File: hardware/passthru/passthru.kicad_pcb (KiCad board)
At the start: 2 copper layers, 63.5 x 59.7 mm, 83 parts, among them J1 ARM_SWD, J2 RJ45_LED_Shielded, J3 Screw_Terminal_01x02, Q1 Q_PMOS_DGS, Q2 Q_PMOS_DGS, Q3 Q_NPN_BEC, U1 EFM32GG11B8xx, U2 KSZ8081RND, U3 LM5085, U4 TPS2375-1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

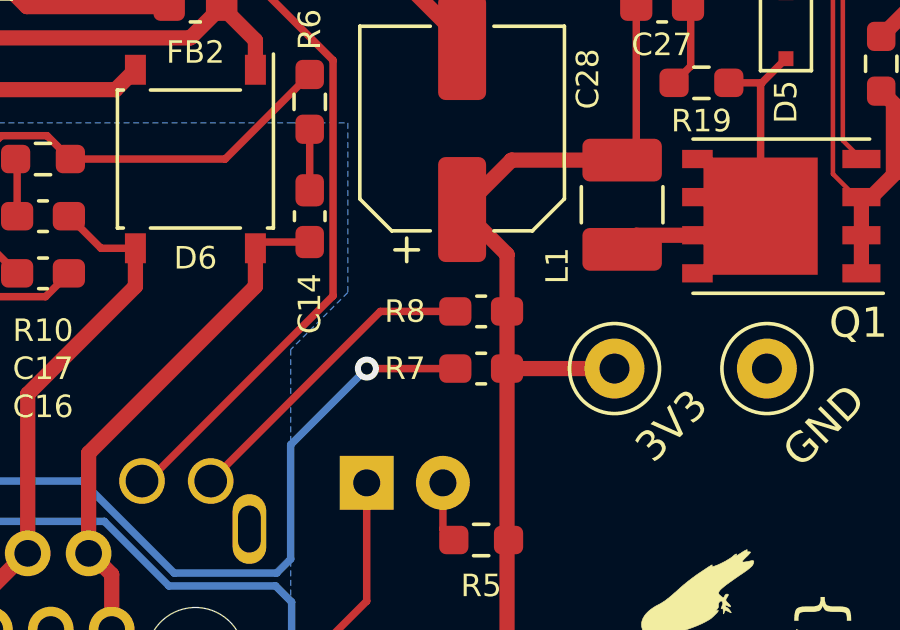
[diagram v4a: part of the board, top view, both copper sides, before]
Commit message: passthru: update resistor values
The 6.1 kΩ resistor was hard to find. I also added the
current-limiting resistors for the LEDs.
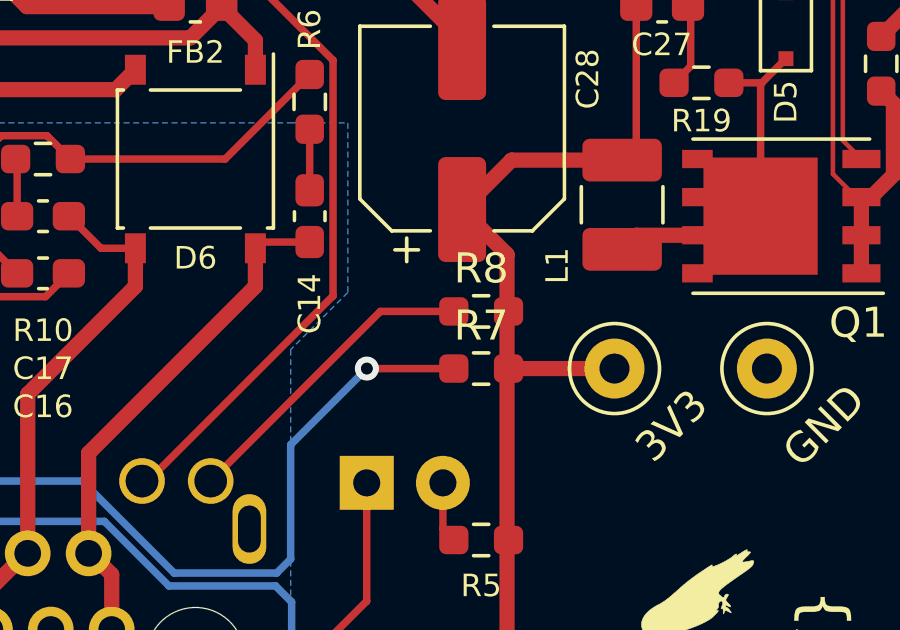
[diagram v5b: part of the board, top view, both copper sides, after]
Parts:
- R20: value 10k -> 16k5
- R21: value 6k1 -> 10k
- R4, R5: value ? -> 68R
- R7, R8: value 65 -> 68R; footprint Capacitor_SMD:C_0603_1608Metric_Pad1.08x0.95mm_HandSolder -> Resistor_SMD:R_0603_1608Metric_Pad0.98x0.95mm_HandSolder
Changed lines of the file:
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@@
       (effects (font (size 0.75 0.75) (thickness 0.15)))
     )
-    (fp_text value "?" (at 0 1.43) (layer "F.Fab")
+    (fp_text value "68R" (at 0 1.43) (layer "F.Fab")
       (effects (font (size 1 1) (thickness 0.15)))
     )
@@
       (effects (font (size 0.75 0.75) (thickness 0.15)))
     )
-    (fp_text value "10k" (at 0 1.43 90) (layer "F.Fab")
+    (fp_text value "16k5" (at 0 1.43 90) (layer "F.Fab")
       (effects (font (size 1 1) (thickness 0.15)))
     )
@@
     )
   )
-  (footprint "Capacitor_SMD:C_0603_1608Metric_Pad1.08x0.95mm_HandSolder" (layer "F.Cu")
+  (footprint "Resistor_SMD:R_0603_1608Metric_Pad0.98x0.95mm_HandSolder" (layer "F.Cu")
     (at 161.925 85.725)
-    (descr "Capacitor SMD 0603 (1608 Metric), square (rectangular) end terminal, IPC_7351 nominal with elongated pad for handsoldering. (Body size source: IPC-SM-782 page 76, https://www.pcb-3d.com/wordpress/wp-content/uploads/ipc-sm-782a_amendment_1_and_2.pdf), generated with kicad-footprint-generator")
-    (tags "capacitor handsolder")
-    (property "Sheetfile" "passthru.kicad_sch")
-    (property "Sheetname" "")
-    (attr smd)
-    (fp_text reference "R8" (at -2.54 0) (layer "F.SilkS")
-      (effects (font (size 0.75 0.75) (thickness 0.15)))
-    )
-    (fp_text value "65" (at 0 1.43) (layer "F.Fab")
-      (effects (font (size 1 1) (thickness 0.15)))
-    )
-    (fp_text user "${REFERENCE}" (at 0 0) (layer "F.Fab")
-      (effects (font (size 0.4 0.4) (thickness 0.06)))
-    )
-    (fp_line (start -0.146267 -0.51) (end 0.146267 -0.51) (layer "F.SilkS") (width 0.12))
-    (fp_line (start -0.146267 0.51) (end 0.146267 0.51) (layer "F.SilkS") (width 0.12))
-    (fp_line (start 1.65 0.73) (end -1.65 0.73) (layer "F.CrtYd") (width 0.05))
-    (fp_line (start 1.65 -0.73) (end 1.65 0.73) (layer "F.CrtYd") (width 0.05))
-    (fp_line (start -1.65 -0.73) (end 1.65 -0.73) (layer "F.CrtYd") (width 0.05))
-    (fp_line (start -1.65 0.73) (end -1.65 -0.73) (layer "F.CrtYd") (width 0.05))
-    (fp_line (start 0.8 -0.4) (end 0.8 0.4) (layer "F.Fab") (width 0.1))
-    (fp_line (start -0.8 0.4) (end -0.8 -0.4) (layer "F.Fab") (width 0.1))
-    (fp_line (start 0.8 0.4) (end -0.8 0.4) (layer "F.Fab") (width 0.1))
-    (fp_line (start -0.8 -0.4) (end 0.8 -0.4) (layer "F.Fab") (width 0.1))
-    (pad "1" smd roundrect (at -0.8625 0) (size 1.075 0.95) (layers "F.Cu" "F.Paste" "F.Mask") (roundrect_rratio 0.25)
+    (descr "Resistor SMD 0603 (1608 Metric), square (rectangular) end terminal, IPC_7351 nominal with elongated pad for handsoldering. (Body size source: IPC-SM-782 page 72, https://www.pcb-3d.com/wordpress/wp-content/uploads/ipc-sm-782a_amendment_1_and_2.pdf), generated with kicad-footprint-generator")
+    (tags "resistor handsolder")
+    (property "Sheetfile" "passthru.kicad_sch")
+    (property "Sheetname" "")
+    (attr smd)
+    (fp_text reference "R8" (at 0 -1.43) (layer "F.SilkS")
+      (effects (font (size 1 1) (thickness 0.15)))
+    )
+    (fp_text value "68R" (at 0 1.43) (layer "F.Fab")
+      (effects (font (size 1 1) (thickness 0.15)))
+    )
+    (fp_text user "${REFERENCE}" (at 0 0) (layer "F.Fab")
+      (effects (font (size 0.4 0.4) (thickness 0.06)))
+    )
+    (fp_line (start -0.254724 0.5225) (end 0.254724 0.5225) (layer "F.SilkS") (width 0.12))
+    (fp_line (start -0.254724 -0.5225) (end 0.254724 -0.5225) (layer "F.SilkS") (width 0.12))
+    (fp_line (start 1.65 0.73) (end -1.65 0.73) (layer "F.CrtYd") (width 0.05))
+    (fp_line (start -1.65 -0.73) (end 1.65 -0.73) (layer "F.CrtYd") (width 0.05))
+    (fp_line (start -1.65 0.73) (end -1.65 -0.73) (layer "F.CrtYd") (width 0.05))
+    (fp_line (start 1.65 -0.73) (end 1.65 0.73) (layer "F.CrtYd") (width 0.05))
+    (fp_line (start 0.8 0.4125) (end -0.8 0.4125) (layer "F.Fab") (width 0.1))
+    (fp_line (start 0.8 -0.4125) (end 0.8 0.4125) (layer "F.Fab") (width 0.1))
+    (fp_line (start -0.8 0.4125) (end -0.8 -0.4125) (layer "F.Fab") (width 0.1))
+    (fp_line (start -0.8 -0.4125) (end 0.8 -0.4125) (layer "F.Fab") (width 0.1))
+    (pad "1" smd roundrect (at -0.9125 0) (size 0.975 0.95) (layers "F.Cu" "F.Paste" "F.Mask") (roundrect_rratio 0.25)
       (net 97 "Net-(J2-Pad12)") (pintype "passive"))
-    (pad "2" smd roundrect (at 0.8625 0) (size 1.075 0.95) (layers "F.Cu" "F.Paste" "F.Mask") (roundrect_rratio 0.25)
+    (pad "2" smd roundrect (at 0.9125 0) (size 0.975 0.95) (layers "F.Cu" "F.Paste" "F.Mask") (roundrect_rratio 0.25)
       (net 10 "+3V3") (pintype "passive"))
-    (model "${KICAD6_3DMODEL_DIR}/Capacitor_SMD.3dshapes/C_0603_1608Metric.wrl"
+    (model "${KICAD6_3DMODEL_DIR}/Resistor_SMD.3dshapes/R_0603_1608Metric.wrl"
       (offset (xyz 0 0 0))
       (scale (xyz 1 1 1))
@@
     )
   )
-  (footprint "Capacitor_SMD:C_0603_1608Metric_Pad1.08x0.95mm_HandSolder" (layer "F.Cu")
+  (footprint "Resistor_SMD:R_0603_1608Metric_Pad0.98x0.95mm_HandSolder" (layer "F.Cu")
     (at 161.925 87.63)
-    (descr "Capacitor SMD 0603 (1608 Metric), square (rectangular) end terminal, IPC_7351 nominal with elongated pad for handsoldering. (Body size source: IPC-SM-782 page 76, https://www.pcb-3d.com/wordpress/wp-content/uploads/ipc-sm-782a_amendment_1_and_2.pdf), generated with kicad-footprint-generator")
-    (tags "capacitor handsolder")
-    (property "Sheetfile" "passthru.kicad_sch")
-    (property "Sheetname" "")
-    (attr smd)
-    (fp_text reference "R7" (at -2.54 0) (layer "F.SilkS")
-      (effects (font (size 0.75 0.75) (thickness 0.15)))
-    )
-    (fp_text value "65" (at 0 1.43) (layer "F.Fab")
-      (effects (font (size 1 1) (thickness 0.15)))
-    )
-    (fp_text user "${REFERENCE}" (at 0 0) (layer "F.Fab")
-      (effects (font (size 0.4 0.4) (thickness 0.06)))
-    )
-    (fp_line (start -0.146267 -0.51) (end 0.146267 -0.51) (layer "F.SilkS") (width 0.12))
-    (fp_line (start -0.146267 0.51) (end 0.146267 0.51) (layer "F.SilkS") (width 0.12))
-    (fp_line (start 1.65 -0.73) (end 1.65 0.73) (layer "F.CrtYd") (width 0.05))
-    (fp_line (start -1.65 0.73) (end -1.65 -0.73) (layer "F.CrtYd") (width 0.05))
-    (fp_line (start -1.65 -0.73) (end 1.65 -0.73) (layer "F.CrtYd") (width 0.05))
-    (fp_line (start 1.65 0.73) (end -1.65 0.73) (layer "F.CrtYd") (width 0.05))
-    (fp_line (start 0.8 -0.4) (end 0.8 0.4) (layer "F.Fab") (width 0.1))
-    (fp_line (start -0.8 0.4) (end -0.8 -0.4) (layer "F.Fab") (width 0.1))
-    (fp_line (start 0.8 0.4) (end -0.8 0.4) (layer "F.Fab") (width 0.1))
-    (fp_line (start -0.8 -0.4) (end 0.8 -0.4) (layer "F.Fab") (width 0.1))
-    (pad "1" smd roundrect (at -0.8625 0) (size 1.075 0.95) (layers "F.Cu" "F.Paste" "F.Mask") (roundrect_rratio 0.25)
+    (descr "Resistor SMD 0603 (1608 Metric), square (rectangular) end terminal, IPC_7351 nominal with elongated pad for handsoldering. (Body size source: IPC-SM-782 page 72, https://www.pcb-3d.com/wordpress/wp-content/uploads/ipc-sm-782a_amendment_1_and_2.pdf), generated with kicad-footprint-generator")
+    (tags "resistor handsolder")
+    (property "Sheetfile" "passthru.kicad_sch")
+    (property "Sheetname" "")
+    (attr smd)
+    (fp_text reference "R7" (at 0 -1.43) (layer "F.SilkS")
+      (effects (font (size 1 1) (thickness 0.15)))
+    )
+    (fp_text value "68R" (at 0 1.43) (layer "F.Fab")
+      (effects (font (size 1 1) (thickness 0.15)))
+    )
+    (fp_text user "${REFERENCE}" (at 0 0) (layer "F.Fab")
+      (effects (font (size 0.4 0.4) (thickness 0.06)))
+    )
+    (fp_line (start -0.254724 0.5225) (end 0.254724 0.5225) (layer "F.SilkS") (width 0.12))
+    (fp_line (start -0.254724 -0.5225) (end 0.254724 -0.5225) (layer "F.SilkS") (width 0.12))
+    (fp_line (start 1.65 -0.73) (end 1.65 0.73) (layer "F.CrtYd") (width 0.05))
+    (fp_line (start -1.65 -0.73) (end 1.65 -0.73) (layer "F.CrtYd") (width 0.05))
+    (fp_line (start -1.65 0.73) (end -1.65 -0.73) (layer "F.CrtYd") (width 0.05))
+    (fp_line (start 1.65 0.73) (end -1.65 0.73) (layer "F.CrtYd") (width 0.05))
+    (fp_line (start -0.8 0.4125) (end -0.8 -0.4125) (layer "F.Fab") (width 0.1))
+    (fp_line (start 0.8 -0.4125) (end 0.8 0.4125) (layer "F.Fab") (width 0.1))
+    (fp_line (start -0.8 -0.4125) (end 0.8 -0.4125) (layer "F.Fab") (width 0.1))
+    (fp_line (start 0.8 0.4125) (end -0.8 0.4125) (layer "F.Fab") (width 0.1))
+    (pad "1" smd roundrect (at -0.9125 0) (size 0.975 0.95) (layers "F.Cu" "F.Paste" "F.Mask") (roundrect_rratio 0.25)
       (net 96 "Net-(J2-Pad10)") (pintype "passive"))
-    (pad "2" smd roundrect (at 0.8625 0) (size 1.075 0.95) (layers "F.Cu" "F.Paste" "F.Mask") (roundrect_rratio 0.25)
+    (pad "2" smd roundrect (at 0.9125 0) (size 0.975 0.95) (layers "F.Cu" "F.Paste" "F.Mask") (roundrect_rratio 0.25)
       (net 10 "+3V3") (pintype "passive"))
-    (model "${KICAD6_3DMODEL_DIR}/Capacitor_SMD.3dshapes/C_0603_1608Metric.wrl"
+    (model "${KICAD6_3DMODEL_DIR}/Resistor_SMD.3dshapes/R_0603_1608Metric.wrl"
       (offset (xyz 0 0 0))
       (scale (xyz 1 1 1))
@@
       (effects (font (size 0.75 0.75) (thickness 0.15)) (justify left))
     )
-    (fp_text value "6k1" (at 0 1.43) (layer "F.Fab")
+    (fp_text value "10k" (at 0 1.43) (layer "F.Fab")
       (effects (font (size 1 1) (thickness 0.15)))
     )
@@
       (effects (font (size 0.75 0.75) (thickness 0.15)))
     )
-    (fp_text value "?" (at 0 1.43) (layer "F.Fab")
-      (effects (font (size 1 1) (thickness 0.15)))
-    )
+    (fp_text value "68R" (at 0 1.43) (layer "F.Fab")
+      (effects (font (size 1 1) (thickness 0.15)))
+    )

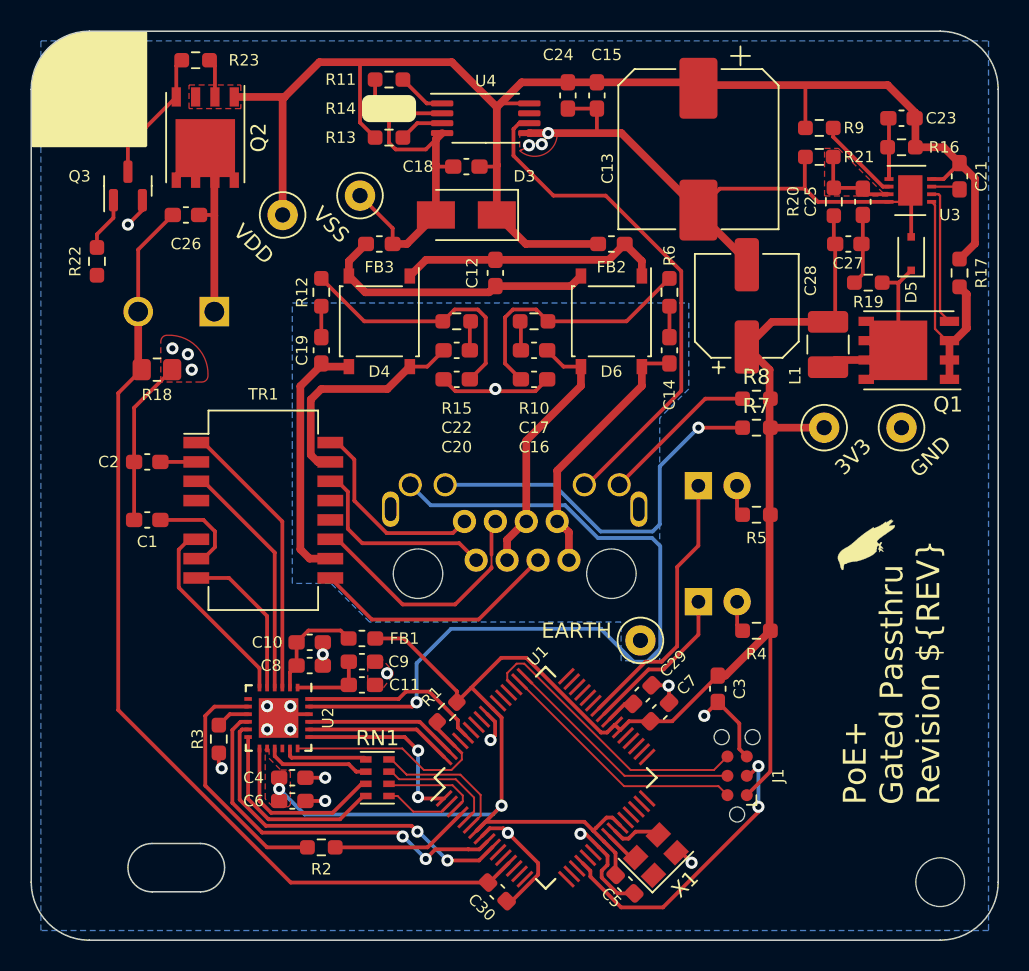
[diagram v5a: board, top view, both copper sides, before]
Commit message: passthru: update footprint for C24
This needs to be larger because of the higher voltage.
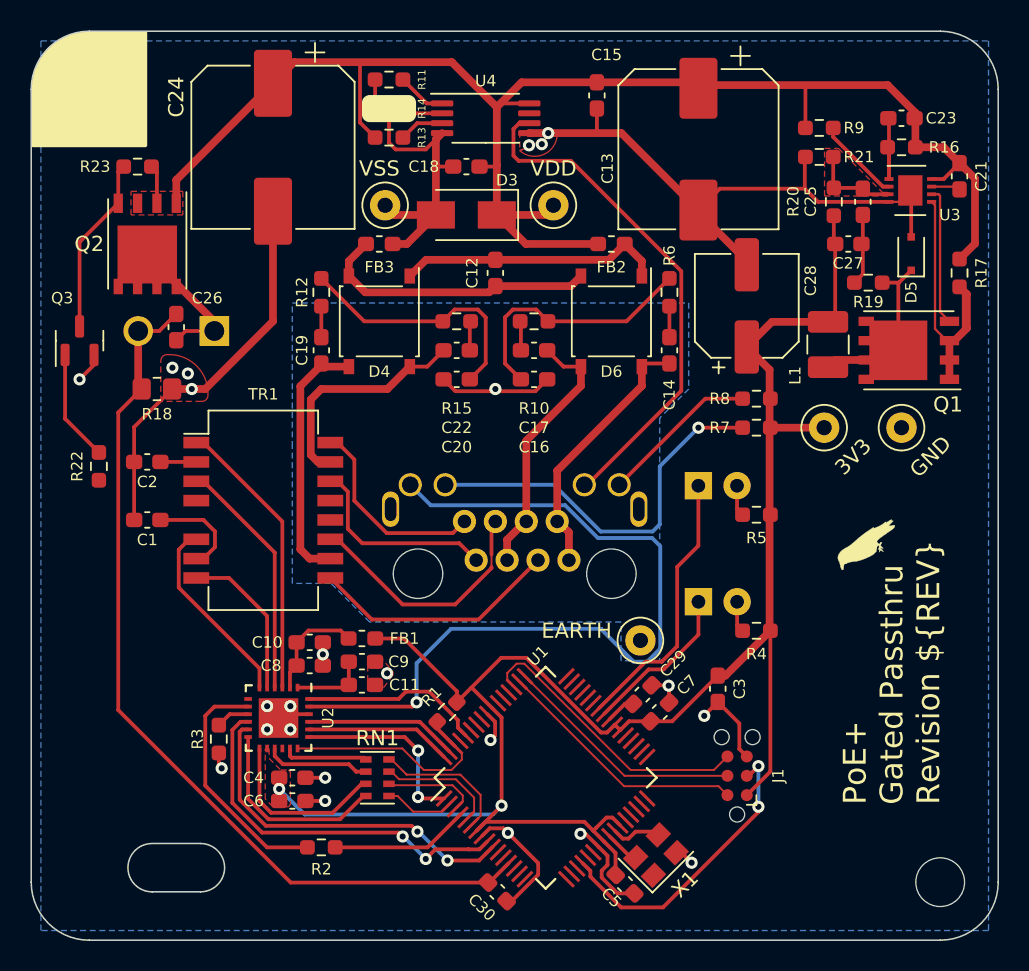
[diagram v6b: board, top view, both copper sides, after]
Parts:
- C24: footprint Capacitor_SMD:C_0603_1608Metric_Pad1.08x0.95mm_HandSolder -> Capacitor_SMD:CP_Elec_10x12.5
- moved C24 19.7 mm to (130.2, 69.2)
- moved TP2 17.8 mm to (148.6, 73.0)
- moved R22 13.5 mm to (118.7, 90.2)
- moved Q3 10.6 mm to (117.5, 81.9)
- moved Q2 7.96 mm to (121.9, 75.6)
- moved R23 7.96 mm to (121.3, 70.5)
- moved C26 7.39 mm to (123.8, 81.0), turned to 90 degrees
- moved TP3 1.77 mm to (137.5, 73.0)
- moved R18 1.27 mm to (122.6, 85.1)
- moved J3 1.27 mm to (123.8, 81.3)
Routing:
- net GND: track 85.7 -> 98.0 mm
- net /LOAD_SEN: track 64.6 -> 59.0 mm
- net VDD: track 99.1 -> 102.8 mm
- net Net-(Q3-Pad1): track 3.55 -> 7.32 mm
- net /LOAD_SW: track 8.78 -> 11.7 mm
- net Net-(C26-Pad1): track 11.2 -> 8.98 mm
- net +3V3: track 122.5 -> 121.7 mm
